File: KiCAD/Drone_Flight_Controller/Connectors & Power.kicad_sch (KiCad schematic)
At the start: 51 parts, among them J301 Conn_01x03_Pin, J302 Conn_01x04, J303 Conn_01x03_Pin, J304 XT60, J305 Conn_01x03_Pin, J306 Conn_01x03_Pin, Q301 BC846C, Q302 BC846C, Q303 BC856C, Q304 BC846C, Q305 BC856C, Q306 BC856C, Q307 BC856C, Q309 BC846C, U202 AS358, U203 AS358, U301 AS358, U302 AS358, U305 AS358

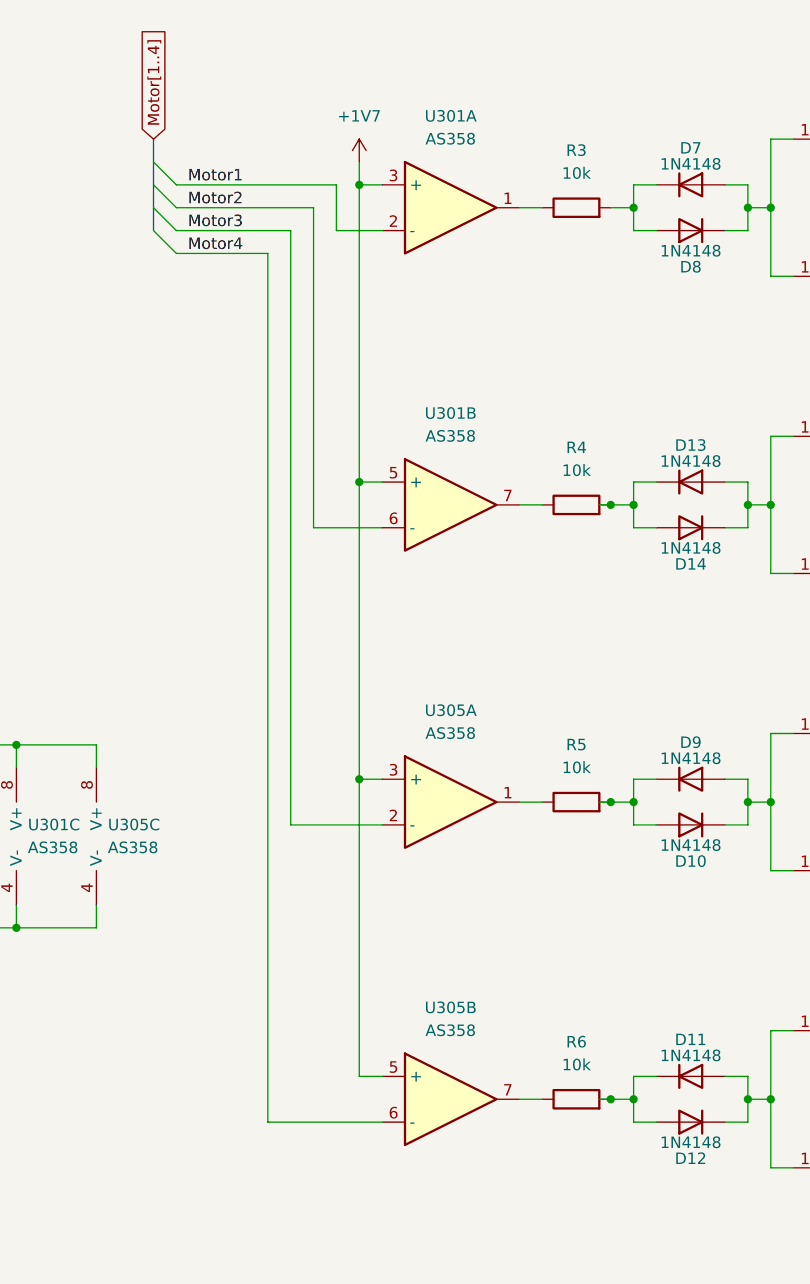
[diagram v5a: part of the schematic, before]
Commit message: Fix error in Commit 28fc275 because of not saving
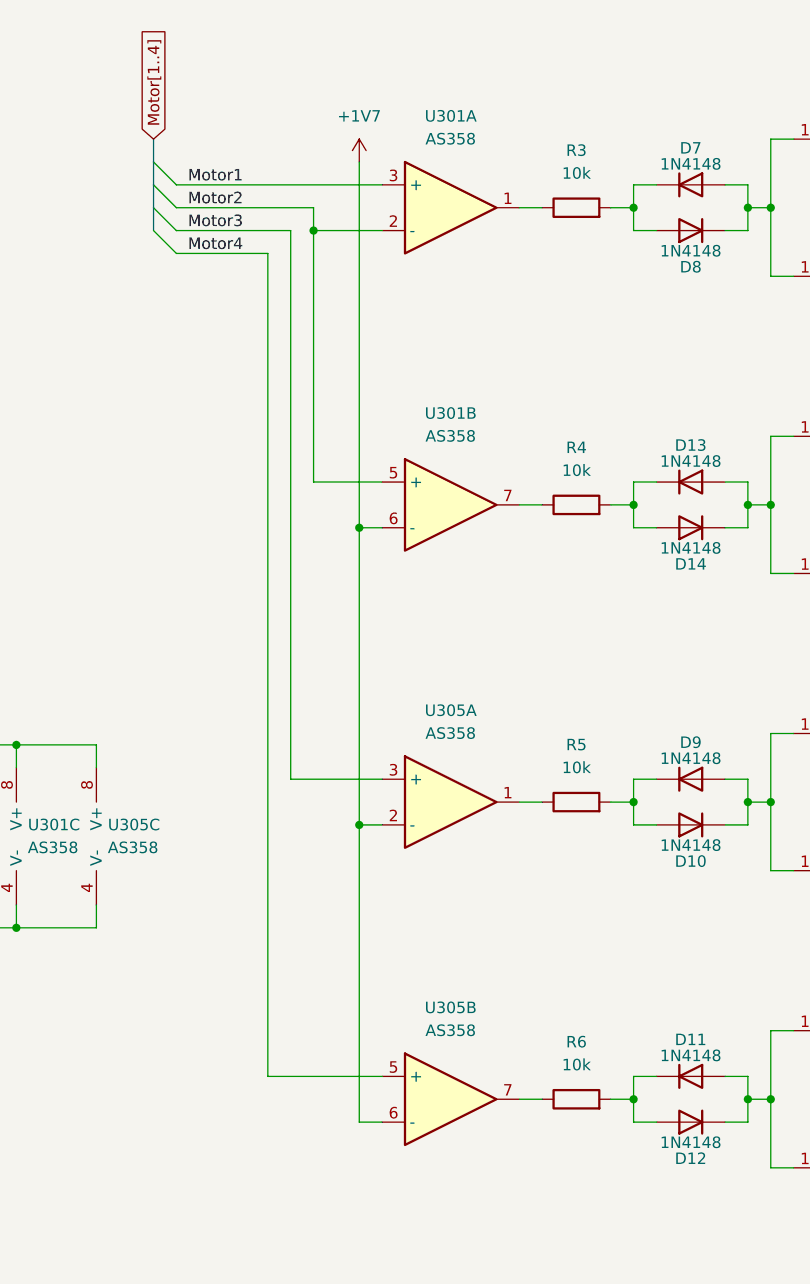
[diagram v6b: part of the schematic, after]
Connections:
- net +1V7: now also U301.6 (-), U305.2 (-), U305.6 (-); no longer U301.3 (+), U301.5 (+), U305.3 (+), U305.5 (+)
- net Motor1: now also U301.3 (+); no longer U301.2 (-)
- net Motor2: now also U301.2 (-), U301.5 (+); no longer U301.6 (-)
- net Motor3: now also U305.3 (+); no longer U305.2 (-)
- net Motor4: now also U305.5 (+); no longer U305.6 (-)

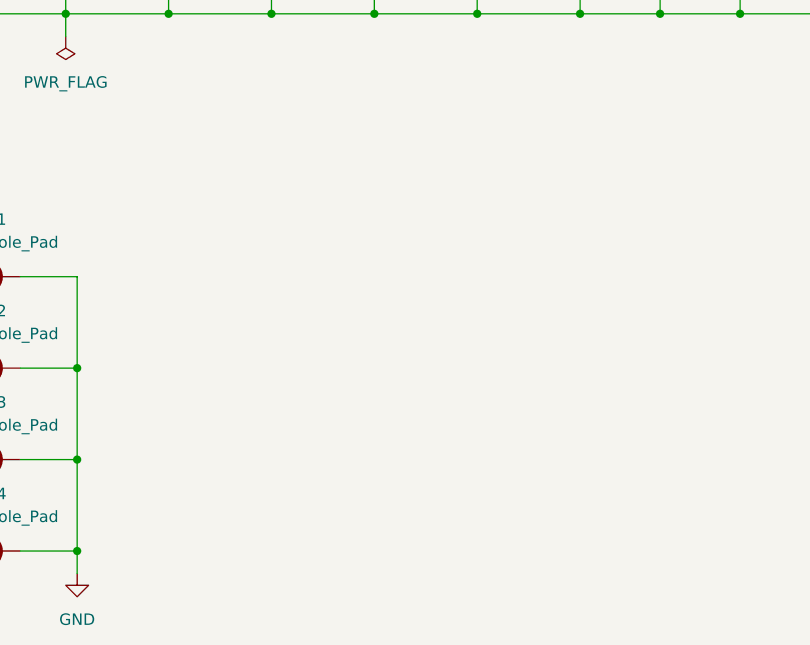
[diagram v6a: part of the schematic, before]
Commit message: Add power indicator LEDs
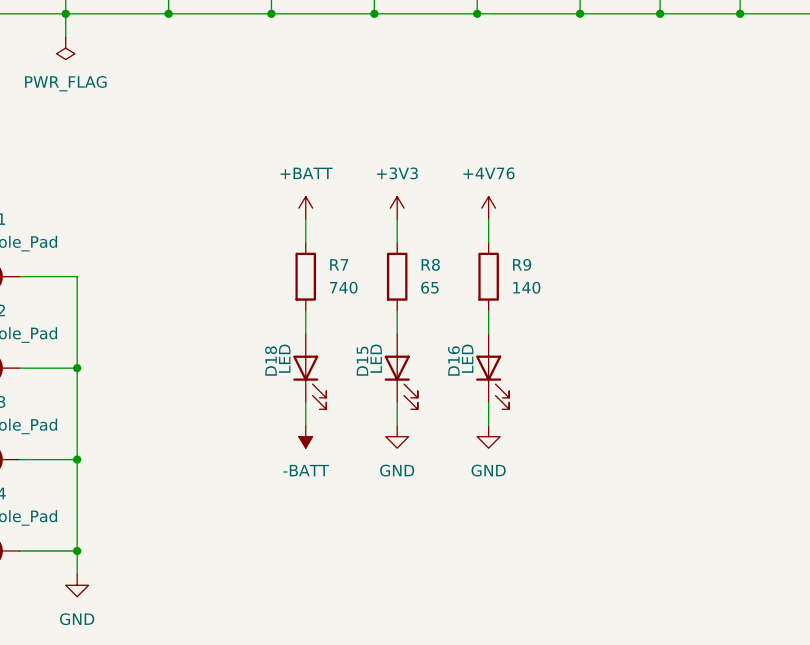
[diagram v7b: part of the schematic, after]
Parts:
- added D15, D16, D18: LED, LED_SMD:LED_0805_2012Metric_Pad1.15x1.40mm_HandSolder, symbol Device:LED
- added R7: 740, symbol Device:R
- added R8: 65, symbol Device:R
- added R9: 140, symbol Device:R
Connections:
- net +4V76: now also R9.1
- net +BATT: now also R7.1
- net -BATT: now also D18.1 (K)
- net GND: now also D15.1 (K), D16.1 (K)
- new net: D18.2 (A), R7.2
- new net: D16.2 (A), R9.2
- new net: D15.2 (A), R8.2
- new net +3V3: R8.1

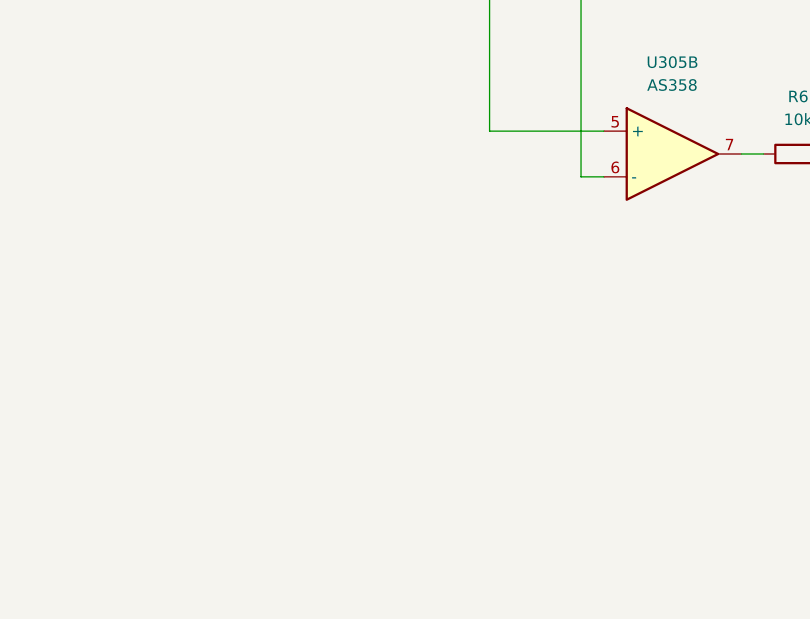
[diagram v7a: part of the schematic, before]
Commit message: Add IO connector
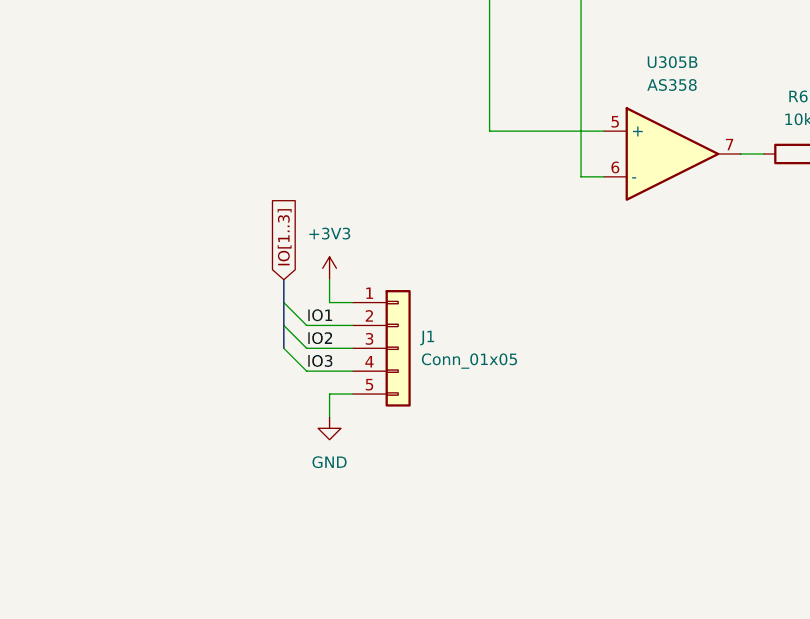
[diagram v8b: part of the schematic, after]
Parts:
- added J1: Conn_01x05, symbol Connector_Generic:Conn_01x05
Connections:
- net +3V3: now also J1.1 (Pin_1)
- net GND: now also J1.5 (Pin_5)
- new net IO1: J1.2 (Pin_2)
- new net IO2: J1.3 (Pin_3)
- new net IO3: J1.4 (Pin_4)
